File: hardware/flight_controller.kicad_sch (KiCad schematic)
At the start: 77 parts, among them IC2 STM32F722RET6, IC3 W25Q128JVSIQ, J1 Conn_01x03, J2 JST SM08B-SRSS-TB(LF)(SN), J3 Conn_01x04, J4 Conn_01x04, J5 Conn_01x04, J6 USB4105-GF-A-060, Q1 TPRT9013-33GB, SW2 KMR221GLFS, U1 BMP581, U2 MP9943GQ-Z, U3 USBLC6-2P6, U4 MP9943GQ-Z, Y2 X322525MOB4SI

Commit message: crystal oscillator
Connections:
- net GND: now also Y2.2 (GND_1); no longer Y2.3 (CRYSTAL__2)
- net HSE_OUT: now also Y2.3 (CRYSTAL__2); no longer Y2.2 (GND_1)
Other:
- moved on the sheet: C36
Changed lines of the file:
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@@
 	)
 	(junction
-		(at 424.18 193.04)
-		(diameter 0)
-		(color 0 0 0 0)
-	)
-	(junction
 		(at 314.96 163.83)
 		(diameter 0)
@@
 	)
 	(junction
+		(at 431.8 190.5)
+		(diameter 0)
+		(color 0 0 0 0)
+	)
+	(junction
 		(at 36.83 248.92)
 		(diameter 0)
@@
 	(wire
 		(pts
-			(xy 424.18 201.93) (xy 424.18 200.66)
-		)
-		(stroke
-			(width 0)
-			(type default)
-		)
-	)
-	(wire
-		(pts
 			(xy 33.02 185.42) (xy 38.1 185.42)
 		)
@@
 	(wire
 		(pts
+			(xy 424.18 200.66) (xy 431.8 200.66)
+		)
+		(stroke
+			(width 0)
+			(type default)
+		)
+	)
+	(wire
+		(pts
 			(xy 372.11 201.93) (xy 372.11 200.66)
 		)
@@
 	(wire
 		(pts
+			(xy 424.18 193.04) (xy 424.18 200.66)
+		)
+		(stroke
+			(width 0)
+			(type default)
+		)
+	)
+	(wire
+		(pts
 			(xy 92.71 33.02) (xy 96.52 33.02)
 		)
@@
 	(wire
 		(pts
+			(xy 419.1 193.04) (xy 424.18 193.04)
+		)
+		(stroke
+			(width 0)
+			(type default)
+		)
+	)
+	(wire
+		(pts
 			(xy 233.68 250.19) (xy 252.73 250.19)
 		)
@@
 	(wire
 		(pts
+			(xy 431.8 190.5) (xy 440.69 190.5)
+		)
+		(stroke
+			(width 0)
+			(type default)
+		)
+	)
+	(wire
+		(pts
 			(xy 57.15 130.81) (xy 100.33 130.81)
 		)
@@
 	(wire
 		(pts
-			(xy 419.1 193.04) (xy 424.18 193.04)
-		)
-		(stroke
-			(width 0)
-			(type default)
-		)
-	)
-	(wire
-		(pts
 			(xy 325.12 114.3) (xy 340.36 114.3)
 		)
@@
 	(wire
 		(pts
-			(xy 431.8 190.5) (xy 431.8 200.66)
+			(xy 431.8 190.5) (xy 431.8 193.04)
 		)
 		(stroke
@@
 	(wire
 		(pts
-			(xy 431.8 200.66) (xy 424.18 200.66)
-		)
-		(stroke
-			(width 0)
-			(type default)
-		)
-	)
-	(wire
-		(pts
 			(xy 369.57 111.76) (xy 382.27 111.76)
 		)
@@
 	(wire
 		(pts
-			(xy 424.18 193.04) (xy 427.99 193.04)
-		)
-		(stroke
-			(width 0)
-			(type default)
-		)
-	)
-	(wire
-		(pts
 			(xy 90.17 110.49) (xy 90.17 111.76)
 		)
@@
 	(wire
 		(pts
+			(xy 424.18 200.66) (xy 424.18 201.93)
+		)
+		(stroke
+			(width 0)
+			(type default)
+		)
+	)
+	(wire
+		(pts
 			(xy 281.94 58.42) (xy 278.13 58.42)
 		)
@@
 		)
 	)
+	(label "HSE_OUT"
+		(at 440.69 190.5 180)
+		(effects
+			(font
+				(size 1.27 1.27)
+			)
+			(justify right bottom)
+		)
+	)
 	(label "ESC_USART_RX"
 		(at 198.12 124.46 180)
@@
 		)
 	)
-	(label "HSE_OUT"
-		(at 427.99 193.04 180)
-		(effects
-			(font
-				(size 1.27 1.27)
-			)
-			(justify right bottom)
-		)
-	)
 	(label "USB_DN"
 		(at 22.86 49.53 0)
@@
 	(symbol
 		(lib_id "Device:C")
-		(at 424.18 196.85 180)
+		(at 431.8 196.85 180)
 		(unit 1)
 		(exclude_from_sim no)
@@
 		(dnp no)
 		(property "Reference" "C36"
-			(at 428.244 194.818 0)
+			(at 435.864 194.818 0)
 			(effects
 				(font
@@
 		)
 		(property "Value" "20pF"
-			(at 423.672 199.644 0)
+			(at 431.292 199.644 0)
 			(effects
 				(font
@@
 		)
 		(property "Footprint" "Capacitor_SMD:C_0402_1005Metric"
-			(at 423.2148 193.04 0)
+			(at 430.8348 193.04 0)
 			(effects
 				(font
@@
 		)
 		(property "Datasheet" "~"
-			(at 424.18 196.85 0)
+			(at 431.8 196.85 0)
 			(effects
 				(font
@@
 		)
 		(property "Description" "Unpolarized capacitor"
-			(at 424.18 196.85 0)
+			(at 431.8 196.85 0)
 			(effects
 				(font

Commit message: fix errors
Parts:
- D1: value ICM-45686 -> LSM6DS3TR
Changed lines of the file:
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@@
 			)
 		)
-		(property "Value" "ICM-45686"
+		(property "Value" "LSM6DS3TR"
 			(at 200.2633 207.01 0)
 			(effects

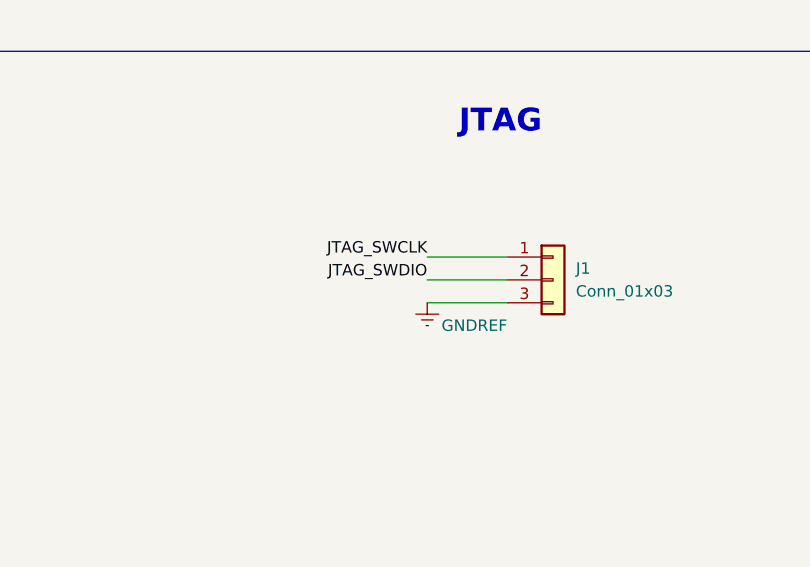
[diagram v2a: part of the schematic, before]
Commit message: jtag interface
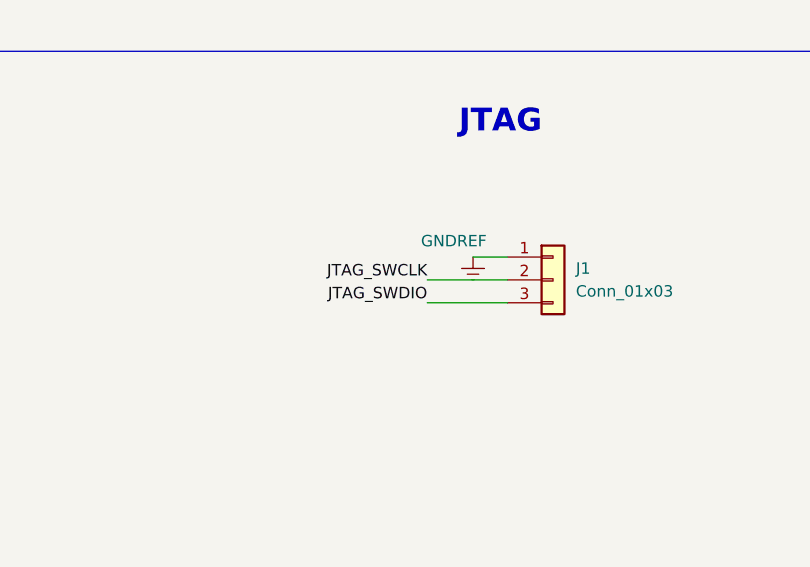
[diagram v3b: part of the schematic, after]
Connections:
- net GND: now also J1.1 (Pin_1); no longer J1.3 (Pin_3)
- net JTAG_SWCLK: now also J1.2 (Pin_2); no longer J1.1 (Pin_1)
- net JTAG_SWDIO: now also J1.3 (Pin_3); no longer J1.2 (Pin_2)
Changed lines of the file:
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@@
 	(wire
 		(pts
+			(xy 392.43 238.76) (xy 396.24 238.76)
+		)
+		(stroke
+			(width 0)
+			(type default)
+		)
+	)
+	(wire
+		(pts
 			(xy 289.56 36.83) (xy 290.83 36.83)
 		)
@@
 	(wire
 		(pts
-			(xy 387.35 238.76) (xy 396.24 238.76)
+			(xy 387.35 241.3) (xy 396.24 241.3)
 		)
 		(stroke
@@
 	(wire
 		(pts
-			(xy 387.35 243.84) (xy 396.24 243.84)
-		)
-		(stroke
-			(width 0)
-			(type default)
-		)
-	)
-	(wire
-		(pts
 			(xy 284.48 55.88) (xy 284.48 71.12)
 		)
@@
 	(wire
 		(pts
-			(xy 387.35 241.3) (xy 396.24 241.3)
+			(xy 387.35 243.84) (xy 396.24 243.84)
 		)
 		(stroke
@@
 	)
 	(label "JTAG_SWDIO"
-		(at 387.35 241.3 180)
+		(at 387.35 243.84 180)
 		(effects
 			(font
@@
 	)
 	(label "JTAG_SWCLK"
-		(at 387.35 238.76 180)
+		(at 387.35 241.3 180)
 		(effects
 			(font
@@
 	(symbol
 		(lib_id "power:GNDREF")
-		(at 387.35 243.84 0)
+		(at 392.43 238.76 0)
 		(unit 1)
 		(exclude_from_sim no)
@@
 		(dnp no)
 		(property "Reference" "#PWR054"
-			(at 387.35 250.19 0)
+			(at 392.43 245.11 0)
 			(effects
 				(font
@@
 		)
 		(property "Value" "GNDREF"
-			(at 396.24 246.38 0)
+			(at 393.954 236.982 0)
 			(effects
 				(font
@@
 		)
 		(property "Footprint" ""
-			(at 387.35 243.84 0)
+			(at 392.43 238.76 0)
 			(effects
 				(font
@@
 		)
 		(property "Datasheet" ""
-			(at 387.35 243.84 0)
+			(at 392.43 238.76 0)
 			(effects
 				(font
@@
 		)
 		(property "Description" "Power symbol creates a global label with name \"GNDREF\" , reference supply ground"
-			(at 387.35 243.84 0)
+			(at 392.43 238.76 0)
 			(effects
 				(font

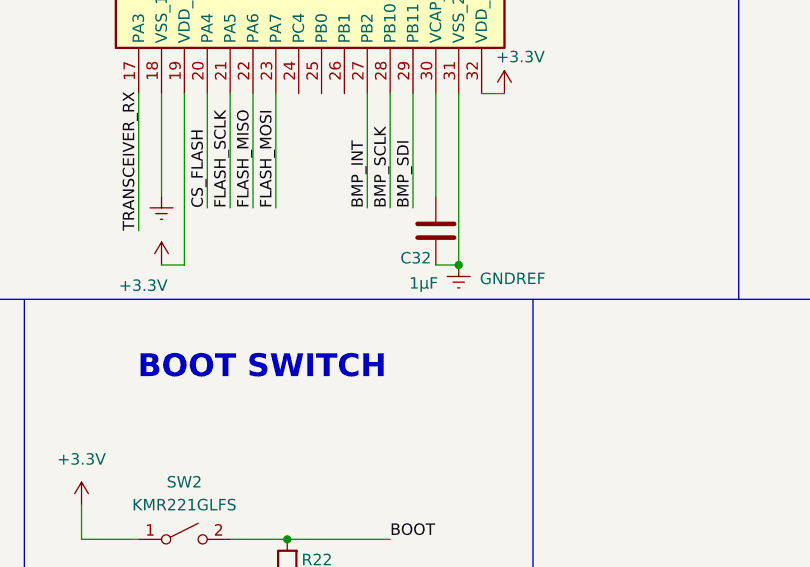
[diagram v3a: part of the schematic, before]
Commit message: changed capacitor
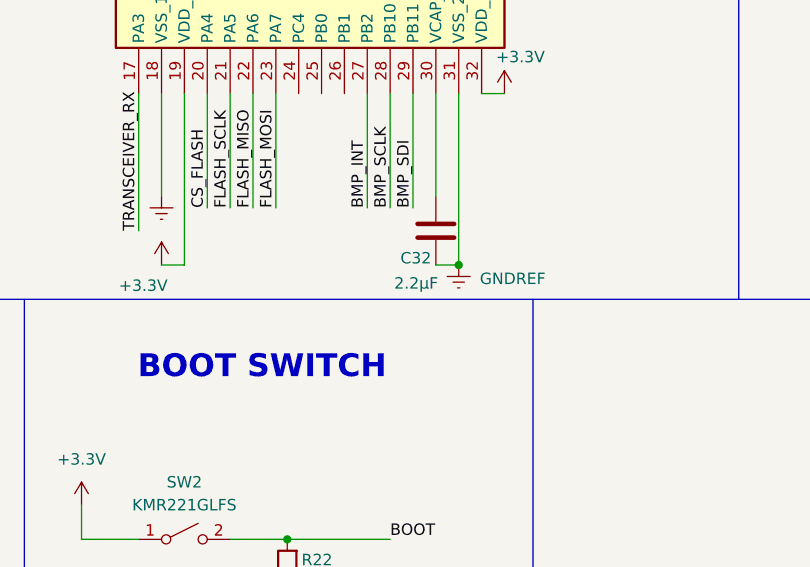
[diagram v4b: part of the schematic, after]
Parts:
- C32: value 1μF -> 2.2μF
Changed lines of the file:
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@@
 			)
 		)
-		(property "Value" "1μF"
+		(property "Value" "2.2μF"
 			(at 312.674 165.862 0)
 			(effects
